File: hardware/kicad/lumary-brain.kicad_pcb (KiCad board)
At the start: 4 copper layers, 63.3 x 31.3 mm, 32 parts, among them J1 PWR_IN, J2 CN1, J3 USB-C, Q1 NMOS_60V, Q2 NMOS_60V, Q3 AO3401A, SW1 BOOT, SW2 EN, U1 ESP32-H2-MINI-1-N4, U2 ME6211C33M5G, U3 74AHCT1G125, U4 USBLC6-2SC6

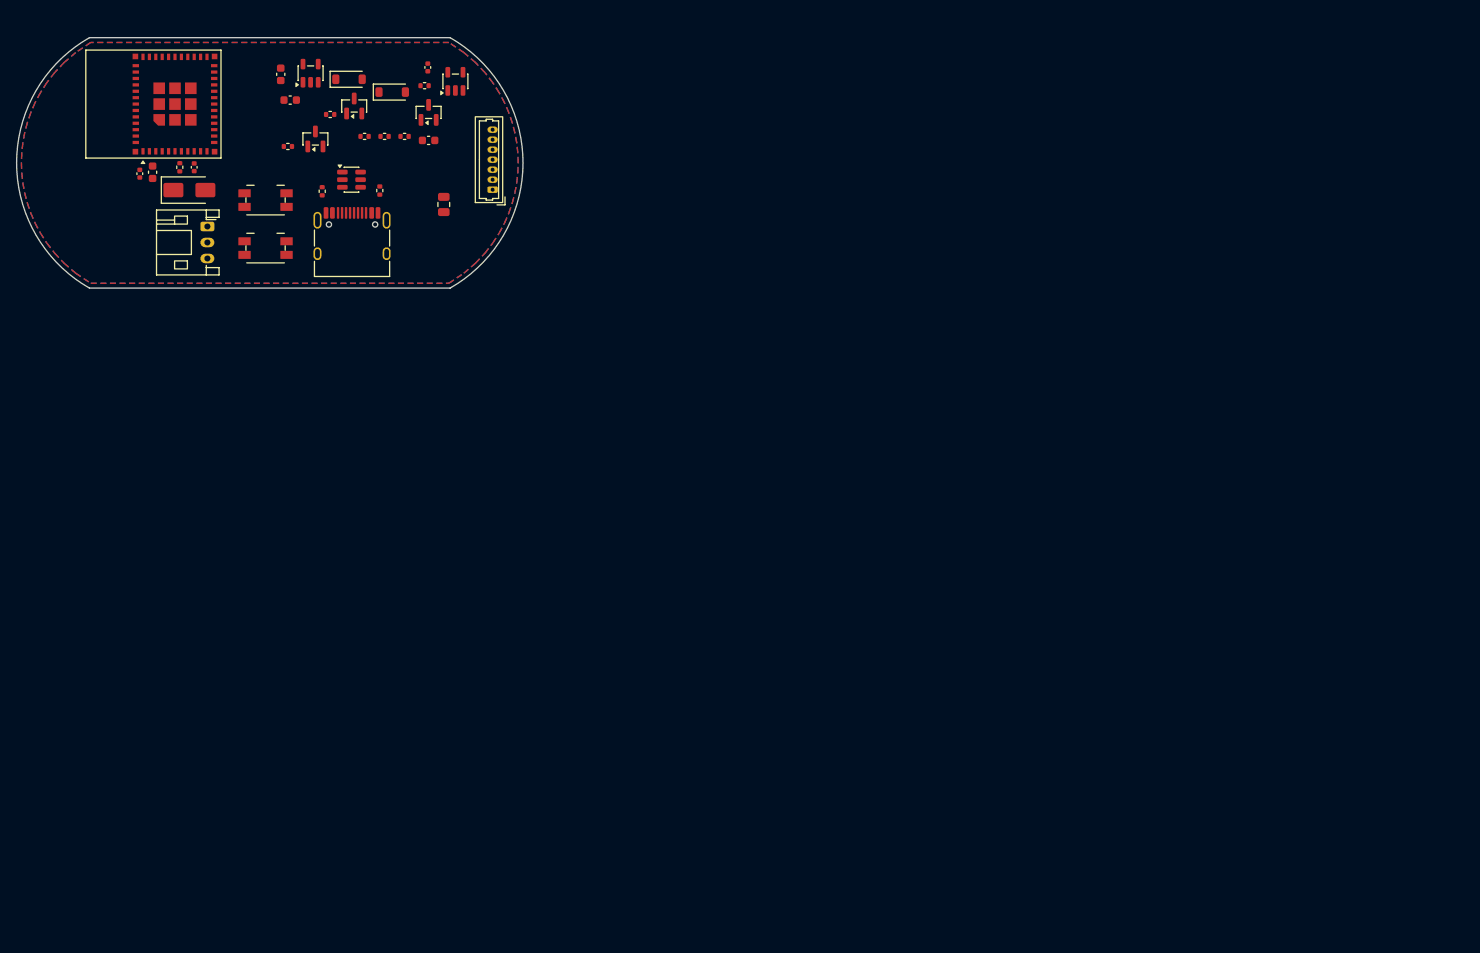
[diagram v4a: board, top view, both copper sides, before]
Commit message: feat(hw): board fully routed, DRC clean
User hand-routed all 49 signal/power airwires; script pass refilled
zones, added 7 GND stitching vias for isolated top-pour islands, and
closed the LDO_IN CE-pin gap (detour below the pad row after a first
attempt shorted across U2's GND pad). Final: 0 violations, 0 unconnected.

NOTE: lumary-brain.kicad_pcb is now the source of truth (contains manual
routing); build_board.py regenerates placement only and would DISCARD
routing if re-run.

Co-Authored-By: Claude Opus 4.8 <noreply@anthropic.com>
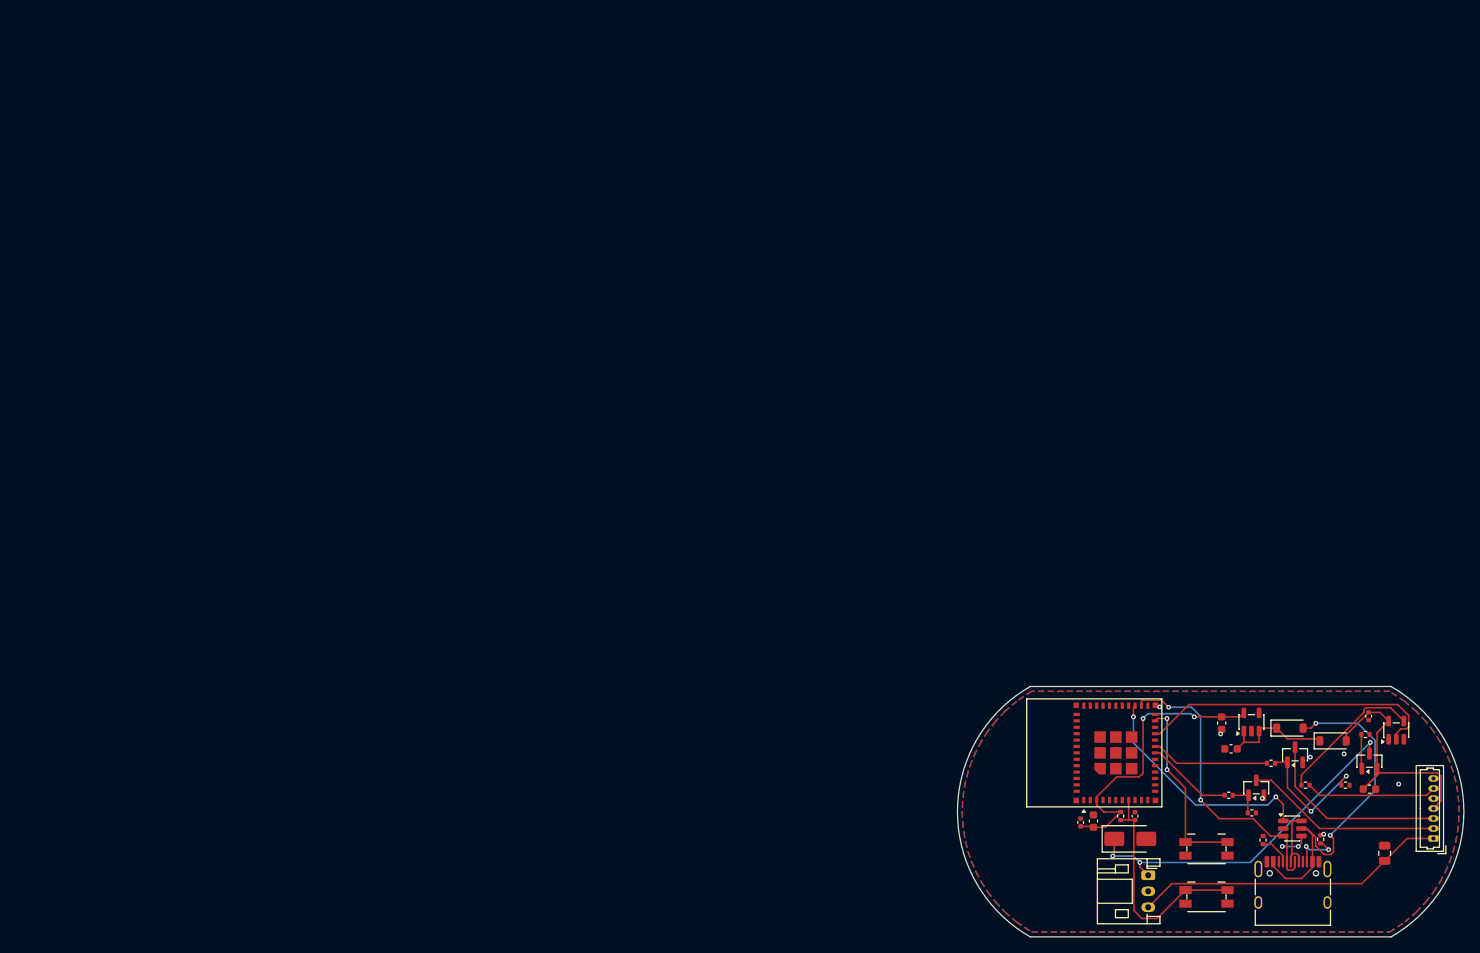
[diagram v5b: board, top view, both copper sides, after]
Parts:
- moved SW1 142.9 mm to (148.7, 101.4)
- moved SW2 142.9 mm to (148.7, 107.4)
- moved C5 142.9 mm to (134.6, 97.9)
- moved U4 142.9 mm to (159.5, 98.8)
- moved Q1 142.9 mm to (155.0, 93.8)
- moved U3 142.9 mm to (172.5, 86.6)
- moved C2 142.9 mm to (150.6, 85.7)
- moved C3 142.9 mm to (151.8, 88.9)
- moved C8 142.9 mm to (139.8, 97.3)
- moved D1 142.9 mm to (164.6, 87.9)
- moved D2 142.9 mm to (159.2, 86.3)
- moved D3 142.9 mm to (139.2, 100.2)
- moved R1 142.9 mm to (151.5, 94.7)
- moved R2 142.9 mm to (156.8, 90.7)
- moved R7 142.9 mm to (155.8, 100.3)
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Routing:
- net +4V7_IN: track 0.00 -> 44.5 mm, vias 0 -> 3
- net VBUS: track 0.00 -> 44.2 mm, vias 0 -> 2
- net USB_DM: track 0.00 -> 41.9 mm, vias 0 -> 4
- net +36V: track 0.00 -> 39.2 mm
- net USB_DP: track 0.00 -> 38.9 mm, vias 0 -> 2
- net RING_DATA_3V3: track 0.00 -> 37.8 mm
- net +3V3: track 0.00 -> 37.3 mm, vias 0 -> 2
- net +4V7: track 0.00 -> 32.7 mm
- net EN: track 0.00 -> 29.3 mm
- net CW_RET: track 0.00 -> 24.6 mm
- net WW_RET: track 0.00 -> 23.8 mm
- net IO9: track 0.00 -> 23.3 mm, vias 0 -> 2
- net RING_BUF_OUT: track 0.00 -> 18.5 mm
- net WW_GATE: track 0.00 -> 16.6 mm, vias 0 -> 2
- net RING_DATA: track 0.00 -> 16.4 mm
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
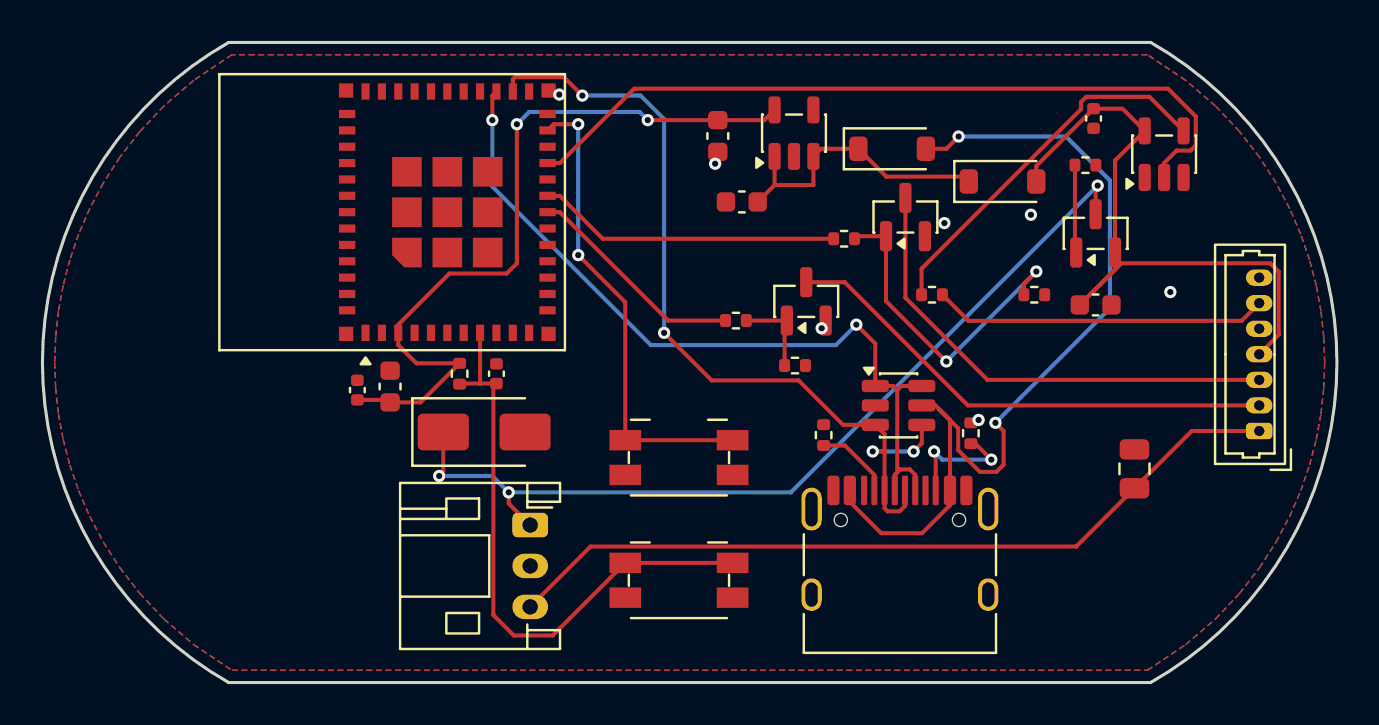
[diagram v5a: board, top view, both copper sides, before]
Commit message: wip: rev B board -- J2 placed, outline shrunk 1mm, routing outstanding
Checkpoint so the KiCad work is in git. The board gate is GREEN on structure --
outline 62.3 x 30.3, J2 footprint, position and all seven pad nets, plus C1 and
Q3 -- and RED on two nets: CW_RET and WW_RET have no routed segments at all,
which is the work still to do.

The outline shrank 0.5mm per side at the user's request because rev A fits the
housing too tightly. That supersedes the spec's 'outline unchanged' item; J2 is
the limiting part and still clears by 1.534mm of copper.

Board-local coordinates all read 0.5mm lower now: the checker takes its origin
from the outline bbox, so the frame moved, not the parts.

Co-Authored-By: Claude Opus 5 <noreply@anthropic.com>
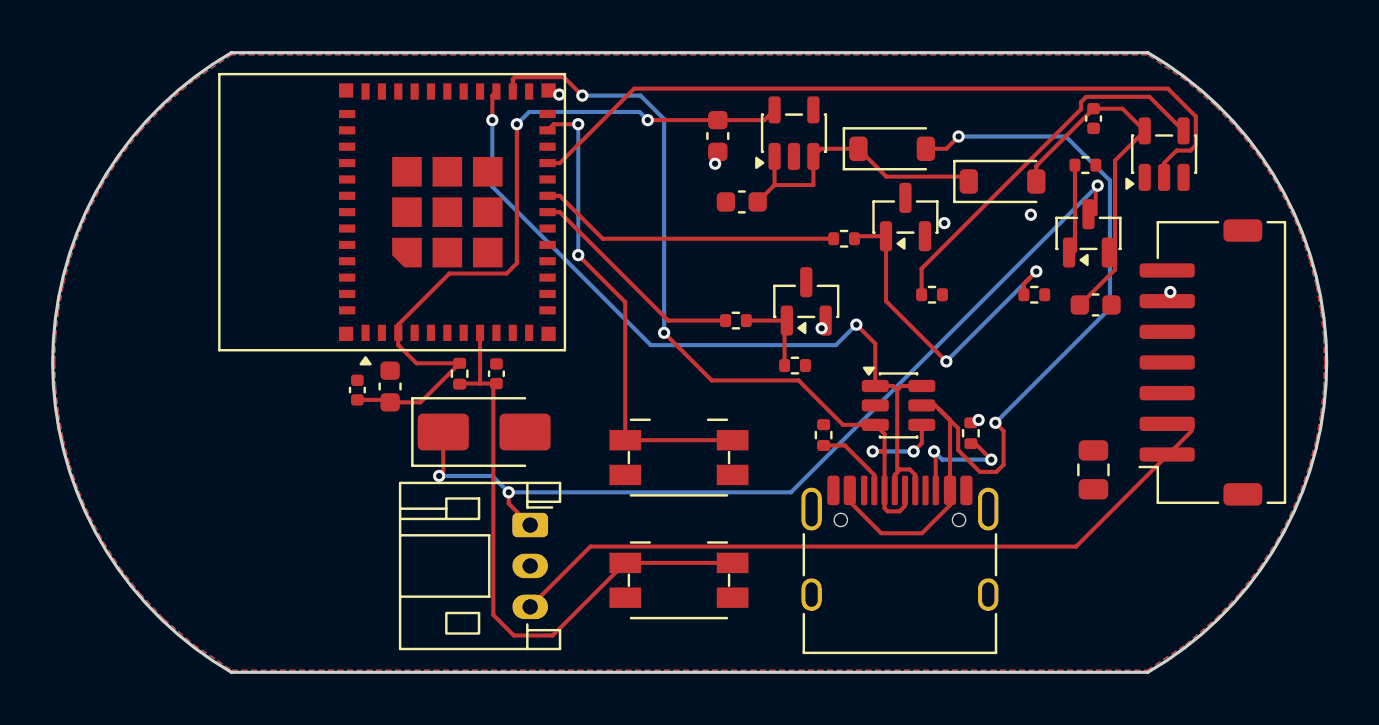
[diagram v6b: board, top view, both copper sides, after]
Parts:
- J2: footprint Connector_Molex:Molex_PicoBlade_53047-0710_1x07_P1.25mm_Vertical -> Connector_JST:JST_ZH_S7B-ZR-SM4A-TF_1x07-1MP_P1.50mm_Horizontal
- moved J2 4.40 mm to (174.3, 96.8)
- moved C1 2.01 mm to (169.0, 102.0)
- moved Q3 0.35 mm to (168.8, 90.4)
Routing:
- net CW_RET: track 24.6 -> 0.00 mm
- net WW_RET: track 23.8 -> 0.00 mm
- net RING_DATA: track 16.4 -> 0.00 mm, vias 0 -> 1
- net +4V7: track 32.7 -> 17.5 mm
- net +36V: track 39.2 -> 35.9 mm
- net GND: vias 7 -> 6
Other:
- board size 63.3 x 31.3 mm -> 62.3 x 30.3 mm

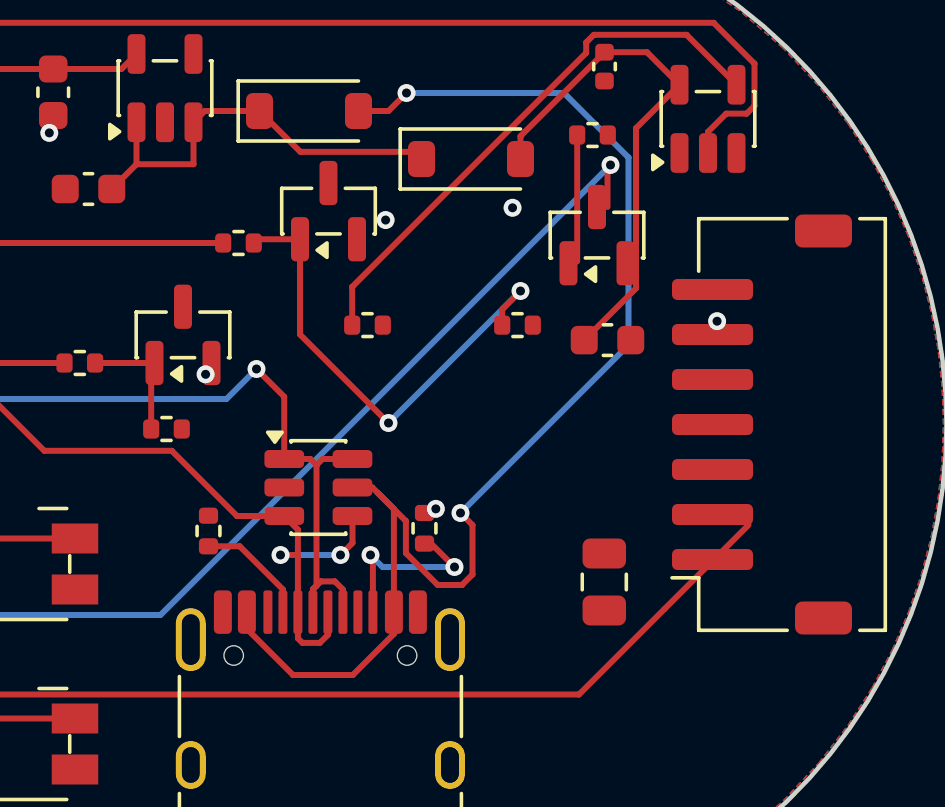
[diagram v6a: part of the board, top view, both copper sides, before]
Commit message: feat: rev B board -- the stock harness now mates, and it is routed
J2 is a JST ZH 1.5mm side-entry connector at board-local (56.15, 15.15) rot 90,
carrying +36V, CW_RET, WW_RET, +4V7, GND and RING_DATA on pads 1-6 with pad 7
unpopulated. C1 and Q3 moved to clear its courtyard, and everything the swap
disturbed is re-routed.

kicad-cli DRC: 0 violations, 0 unconnected items. The +36V stub that ran to the
old J2 position -- which shorted 36V onto the CW_RET pin -- is gone.

C1 is recorded at its as-placed (50.8926, 20.45); it drifted 0.05mm in Y during
routing, which is harmless and now expected by the checker rather than silently
tolerated.

Co-Authored-By: Claude Opus 5 <noreply@anthropic.com>
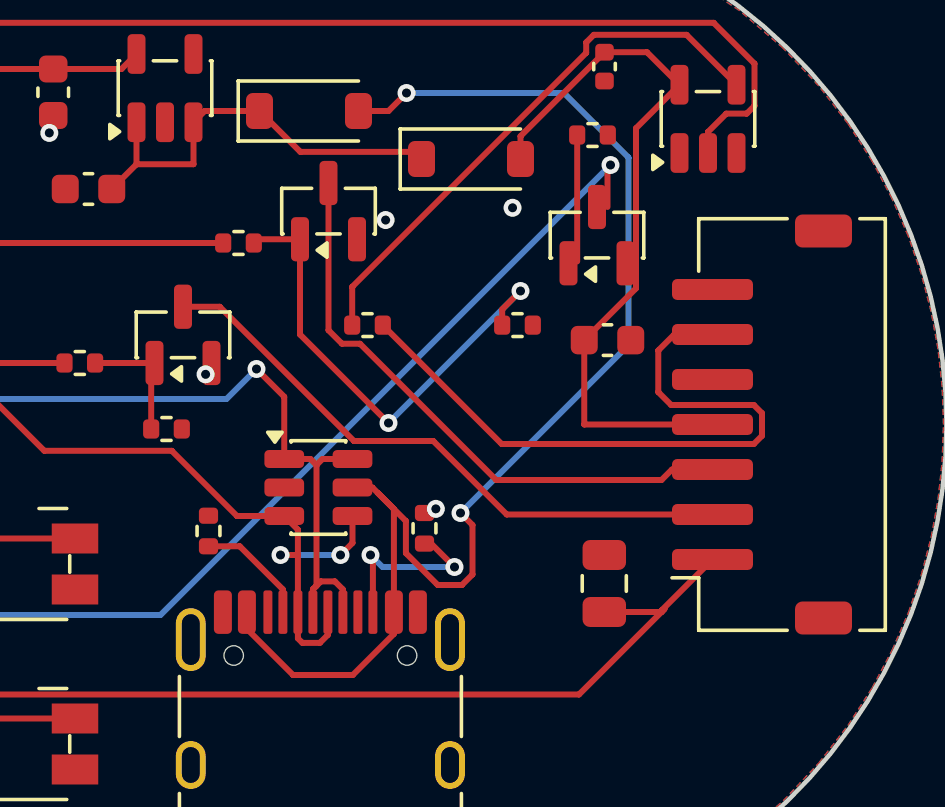
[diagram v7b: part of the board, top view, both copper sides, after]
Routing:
- net RING_DATA: track 0.00 -> 22.3 mm, vias 1 -> 0
- net CW_RET: track 0.00 -> 20.5 mm
- net WW_RET: track 0.00 -> 19.9 mm
- net +4V7: track 17.5 -> 24.6 mm
- net +36V: track 35.9 -> 36.5 mm
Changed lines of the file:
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@@
 	(footprint "Capacitor_SMD:C_0805_2012Metric"
 		(layer "F.Cu")
-		(at 169 102 90)
+		(at 169 102.05 90)
 		(descr "Capacitor SMD 0805 (2012 Metric), square (rectangular) end terminal, IPC-7351 nominal, (Body size source: IPC-SM-782 page 76, https://www.pcb-3d.com/wordpress/wp-content/uploads/ipc-sm-782a_amendment_1_and_2.pdf, https://docs.google.com/spreadsheets/d/1BsfQQcO9C6DZCsRaXUlFlo91Tg2WpOkGARC1WS5S8t0/edit?usp=sharing)")
 		(tags "capacitor")
@@
 	)
 	(segment
+		(start 168.332447 96.75)
+		(end 168.332447 93.9375)
+		(width 0.2)
+		(layer "F.Cu")
+		(net "+4V7")
+	)
+	(segment
 		(start 170.422447 84.34)
 		(end 169.007447 84.34)
@@
 	)
 	(segment
+		(start 172.607447 96.75)
+		(end 168.332447 96.75)
+		(width 0.2)
+		(layer "F.Cu")
+		(net "+4V7")
+	)
+	(segment
 		(start 171.507447 85.425)
 		(end 170.057447 86.875)
@@
 	)
 	(segment
+		(start 170.907447 102.95)
+		(end 172.607447 101.25)
+		(width 0.2)
+		(layer "F.Cu")
+		(net "+36V")
+	)
+	(segment
+		(start 170.907447 103)
+		(end 171.007447 102.9)
+		(width 0.2)
+		(layer "F.Cu")
+		(net "+36V")
+	)
+	(segment
 		(start 144.407447 105.75)
 		(end 141.457447 108.7)
@@
 	)
 	(segment
-		(start 173.807447 100.1)
-		(end 171.007447 102.9)
+		(start 170.907447 103)
+		(end 170.907447 102.95)
 		(width 0.2)
 		(layer "F.Cu")
@@
 		(net "+36V")
 	)
-	(via
-		(at 172.76027 93.30625)
-		(size 0.6)
-		(drill 0.3)
-		(layers "F.Cu" "B.Cu")
+	(segment
+		(start 169 103)
+		(end 170.907447 103)
+		(width 0.2)
+		(layer "F.Cu")
+		(net "+36V")
+	)
+	(segment
+		(start 160.655976 97.3)
+		(end 156.180976 92.825)
+		(width 0.2)
+		(layer "F.Cu")
+		(net "CW_RET")
+	)
+	(segment
+		(start 172.607447 99.75)
+		(end 165.75 99.75)
+		(width 0.2)
+		(layer "F.Cu")
+		(net "CW_RET")
+	)
+	(segment
+		(start 163.3 97.3)
+		(end 160.655976 97.3)
+		(width 0.2)
+		(layer "F.Cu")
+		(net "CW_RET")
+	)
+	(segment
+		(start 156.180976 92.825)
+		(end 154.957447 92.825)
+		(width 0.2)
+		(layer "F.Cu")
+		(net "CW_RET")
+	)
+	(segment
+		(start 165.75 99.75)
+		(end 163.3 97.3)
+		(width 0.2)
+		(layer "F.Cu")
+		(net "CW_RET")
+	)
+	(segment
+		(start 160.8575 94.0575)
+		(end 165.4 98.6)
+		(width 0.2)
+		(layer "F.Cu")
+		(net "WW_RET")
+	)
+	(segment
+		(start 159.807447 88.7)
+		(end 159.807447 93.607447)
+		(width 0.2)
+		(layer "F.Cu")
+		(net "WW_RET")
+	)
+	(segment
+		(start 171.257447 98.25)
+		(end 172.607447 98.25)
+		(width 0.2)
+		(layer "F.Cu")
+		(net "WW_RET")
+	)
+	(segment
+		(start 170.907447 98.6)
+		(end 171.257447 98.25)
+		(width 0.2)
+		(layer "F.Cu")
+		(net "WW_RET")
+	)
+	(segment
+		(start 165.4 98.6)
+		(end 170.907447 98.6)
+		(width 0.2)
+		(layer "F.Cu")
+		(net "WW_RET")
+	)
+	(segment
+		(start 160.2575 94.0575)
+		(end 160.8575 94.0575)
+		(width 0.2)
+		(layer "F.Cu")
+		(net "WW_RET")
+	)
+	(segment
+		(start 159.807447 93.607447)
+		(end 160.2575 94.0575)
+		(width 0.2)
+		(layer "F.Cu")
+		(net "WW_RET")
+	)
+	(segment
+		(start 174.257447 97.126602)
+		(end 173.984049 97.4)
+		(width 0.2)
+		(layer "F.Cu")
+		(net "RING_DATA")
+	)
+	(segment
+		(start 172.607447 93.75)
+		(end 171.332447 93.75)
+		(width 0.2)
+		(layer "F.Cu")
+		(net "RING_DATA")
+	)
+	(segment
+		(start 171.230845 96.1)
+		(end 173.984049 96.1)
+		(width 0.2)
+		(layer "F.Cu")
+		(net "RING_DATA")
+	)
+	(segment
+		(start 171.332447 93.75)
+		(end 170.8 94.282447)
+		(width 0.2)
+		(layer "F.Cu")
+		(net "RING_DATA")
+	)
+	(segment
+		(start 170.8 95.669155)
+		(end 171.230845 96.1)
+		(width 0.2)
+		(layer "F.Cu")
+		(net "RING_DATA")
+	)
+	(segment
+		(start 173.984049 96.1)
+		(end 174.257447 96.373398)
+		(width 0.2)
+		(layer "F.Cu")
+		(net "RING_DATA")
+	)
+	(segment
+		(start 173.984049 97.4)
+		(end 165.579947 97.4)
+		(width 0.2)
+		(layer "F.Cu")
+		(net "RING_DATA")
+	)
+	(segment
+		(start 165.579947 97.4)
+		(end 161.617447 93.4375)
+		(width 0.2)
+		(layer "F.Cu")
+		(net "RING_DATA")
+	)
+	(segment
+		(start 174.257447 96.373398)
+		(end 174.257447 97.126602)
+		(width 0.2)
+		(layer "F.Cu")
+		(net "RING_DATA")
+	)
+	(segment
+		(start 170.8 94.282447)
+		(end 170.8 95.669155)
+		(width 0.2)
+		(layer "F.Cu")
 		(net "RING_DATA")
 	)
